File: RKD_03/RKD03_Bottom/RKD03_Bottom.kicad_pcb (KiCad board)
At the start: 2 copper layers, 97.7 x 97.6 mm, 5 parts

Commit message: RKD03 AddName
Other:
- board text added: "RKD03_v2.0"
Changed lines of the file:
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@@
 		(layer "Edge.Cuts")
 	)
+	(gr_text "RKD03_v2.0"
+		(at 59.53125 95.25 0)
+		(layer "B.SilkS")
+		(effects
+			(font
+				(size 1 1)
+				(thickness 0.1)
+			)
+			(justify left bottom mirror)
+		)
+	)
 )

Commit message: RKD03 プロット
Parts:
- added SW2: KEY_SWITCH, kbd_SW:CherryMX_stab_2u, F.Cu at (121.4, 102.4)
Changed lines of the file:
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@@
+		)
+	)
+	(footprint "kbd_SW:CherryMX_stab_2u"
+		(layer "F.Cu")
+		(at 121.44375 102.39375 180)
+		(property "Reference" "SW2"
+			(at 7 8.1 0)
+			(layer "F.SilkS")
+			(hide yes)
+			(effects
+				(font
+					(size 1 1)
+					(thickness 0.15)
+				)
+			)
+		)
+		(property "Value" "KEY_SWITCH"
+			(at -7.4 -8.1 0)
+			(layer "F.Fab")
+			(hide yes)
+			(effects
+				(font
+					(size 1 1)
+					(thickness 0.15)
+				)
+			)
+		)
+		(property "Footprint" "kbd_SW:CherryMX_stab_2u"
+			(at 0 0 0)
+			(layer "F.Fab")
+			(hide yes)
+			(effects
+				(font
+					(size 1.27 1.27)
+					(thickness 0.15)
+				)
+			)
+		)
+		(property "Datasheet" ""
+			(at 0 0 0)
+			(layer "F.Fab")
+			(hide yes)
+			(effects
+				(font
+					(size 1.27 1.27)
+					(thickness 0.15)
+				)
+			)
+		)
+		(property "Description" ""
+			(at 0 0 0)
+			(layer "F.Fab")
+			(hide yes)
+			(effects
+				(font
+					(size 1.27 1.27)
+					(thickness 0.15)
+				)
+			)
+		)
+		(attr smd)
+		(fp_line
+			(start 18 9)
+			(end -18 9)
+			(stroke
+				(width 0.15)
+				(type solid)
+			)
+			(layer "Eco2.User")
+		)
+		(fp_line
+			(start 18 -9)
+			(end 18 9)
+			(stroke
+				(width 0.15)
+				(type solid)
+			)
+			(layer "Eco2.User")
+		)
+		(fp_line
+			(start -18 9)
+			(end -18 -9)
+			(stroke
+				(width 0.15)
+				(type solid)
+			)
+			(layer "Eco2.User")
+		)
+		(fp_line
+			(start -18 -9)
+			(end 18 -9)
+			(stroke
+				(width 0.15)
+				(type solid)
+			)
+			(layer "Eco2.User")
+		)
+		(fp_line
+			(start 19.025 9.525)
+			(end 19.025 -9.525)
+			(stroke
+				(width 0.15)
+				(type solid)
+			)
+			(layer "F.Fab")
+		)
+		(fp_line
+			(start 19.025 -9.525)
+			(end -19.025 -9.525)
+			(stroke
+				(width 0.15)
+				(type solid)
+			)
+			(layer "F.Fab")
+		)
+		(fp_line
+			(start -19.025 9.525)
+			(end 19.025 9.525)
+			(stroke
+				(width 0.15)
+				(type solid)
+			)
+			(layer "F.Fab")
+		)
+		(fp_line
+			(start -19.025 -9.525)
+			(end -19.025 9.525)
+			(stroke
+				(width 0.15)
+				(type solid)
+			)
+			(layer "F.Fab")
+		)
+		(pad "" np_thru_hole circle
+			(at -11.938 -6.985)
+			(size 3.048 3.048)
+			(drill 3.048)
+			(layers "*.Cu" "*.Mask")
+		)
+		(pad "" np_thru_hole circle
+			(at -11.938 8.255)
+			(size 3.9878 3.9878)
+			(drill 3.9878)
+			(layers "*.Cu" "*.Mask")
+		)
+		(pad "" np_thru_hole circle
+			(at 11.938 -6.985)
+			(size 3.048 3.048)
+			(drill 3.048)
+			(layers "*.Cu" "*.Mask")
+		)
+		(pad "" np_thru_hole circle
+			(at 11.938 8.255)
+			(size 3.9878 3.9878)
+			(drill 3.9878)
+			(layers "*.Cu" "*.Mask")
 		)
 	)

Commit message: RKD03修正
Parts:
- added SW2: KEY_SWITCH, kbd_SW:CherryMX_stab_2u, F.Cu at (73.8, 73.8)
- added SW2: KEY_SWITCH, kbd_SW:CherryMX_stab_2u, F.Cu at (111.9, 73.8)
- added SW2: KEY_SWITCH, kbd_SW:CherryMX_stab_2u, F.Cu at (92.9, 73.8)
- added SW2: KEY_SWITCH, kbd_SW:CherryMX_stab_2u, F.Cu at (54.8, 73.8)
- moved SW2 30.1 mm to (131.0, 73.8), turned to -90 degrees

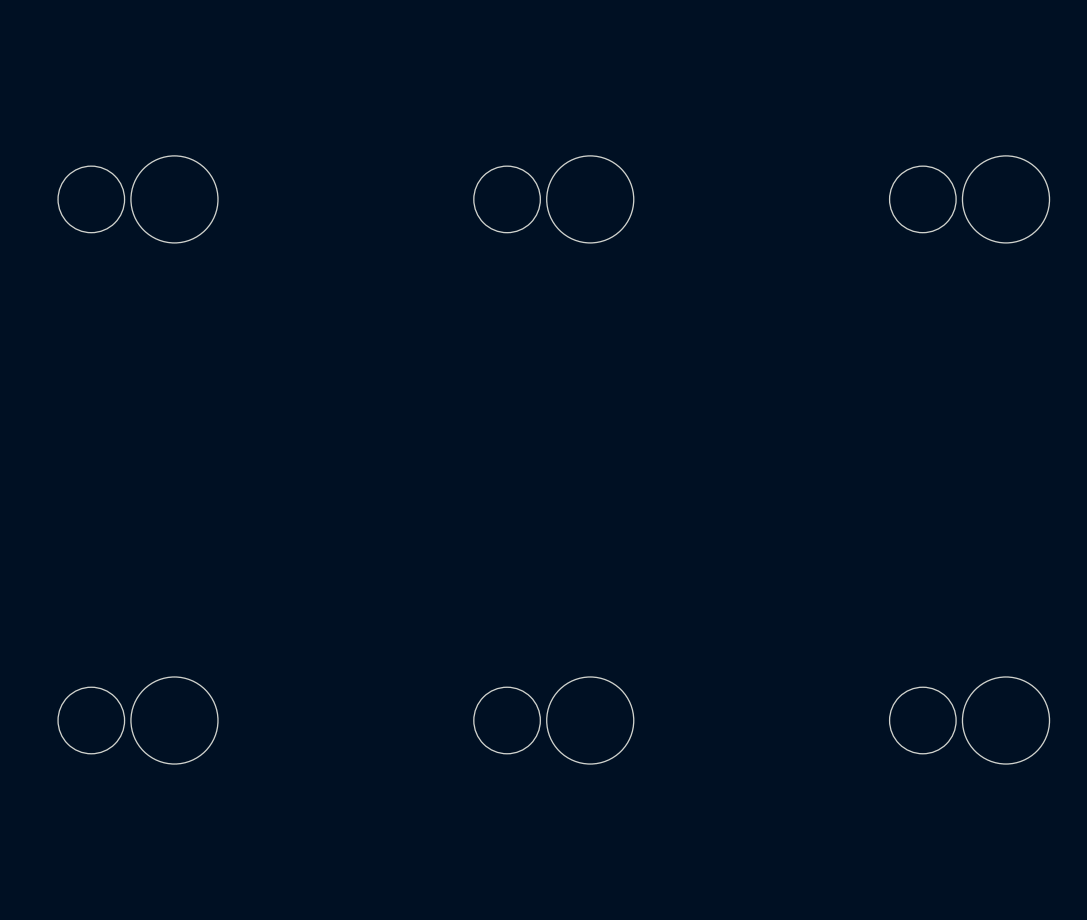
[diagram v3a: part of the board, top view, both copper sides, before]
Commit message: RKD03 2u修正
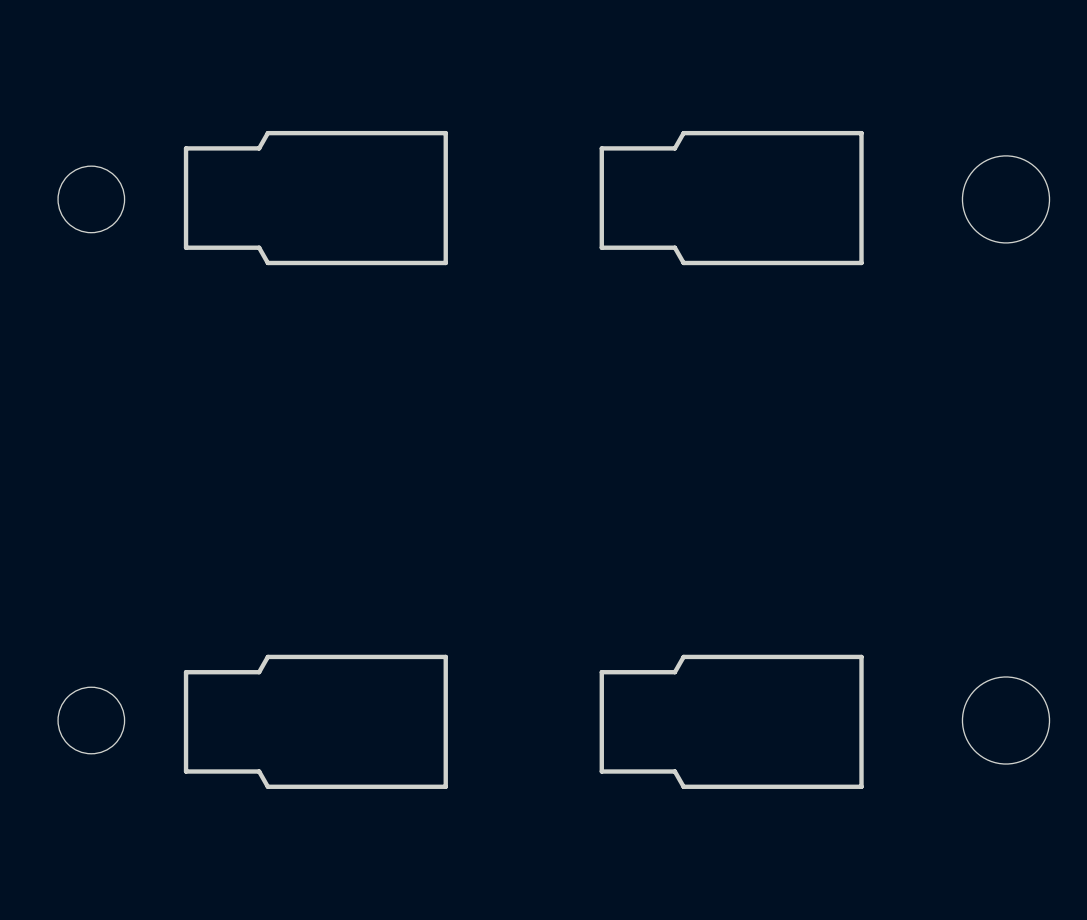
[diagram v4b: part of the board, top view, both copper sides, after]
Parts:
- SW2 (x2): footprint kbd_SW:CherryMX_stab_2u -> Rikkodo_FootPrint:rkd_Bot_ChocV2_2u
- turned SW2 to 90 degrees (x2)

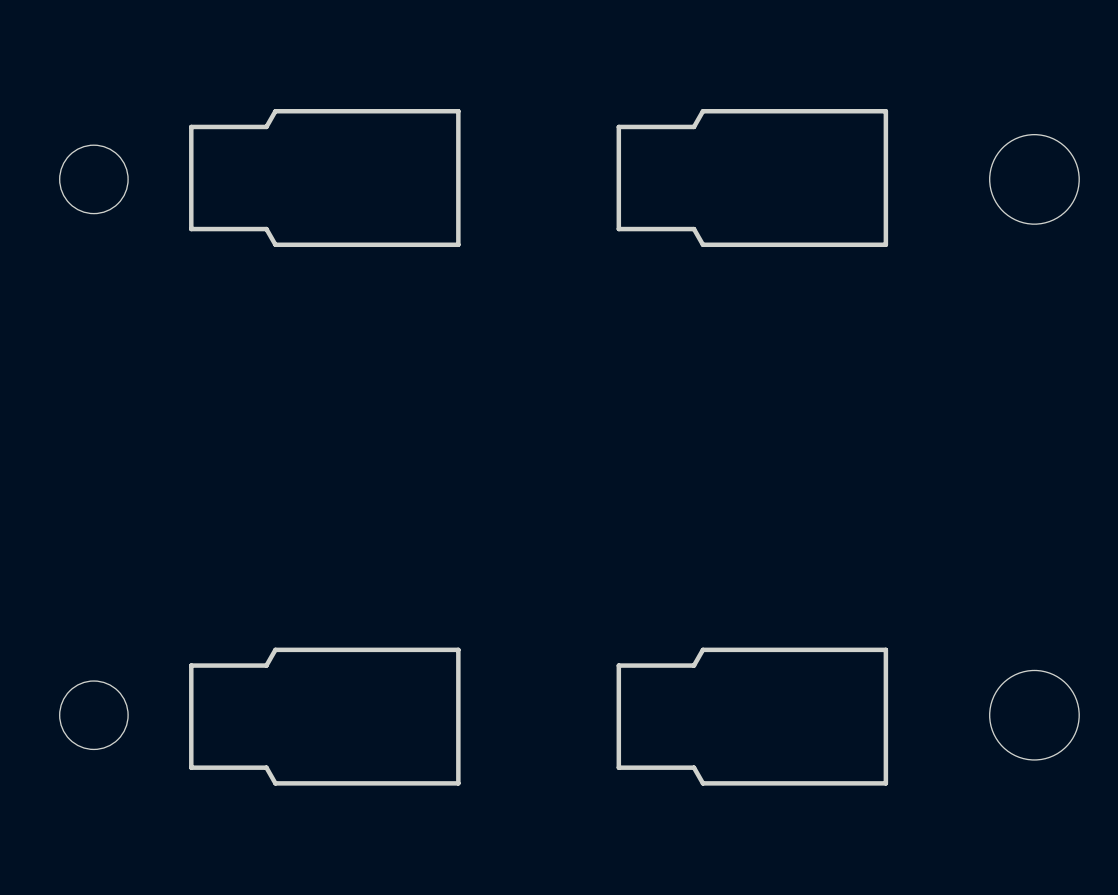
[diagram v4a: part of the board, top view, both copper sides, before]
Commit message: RKD03 部品修正
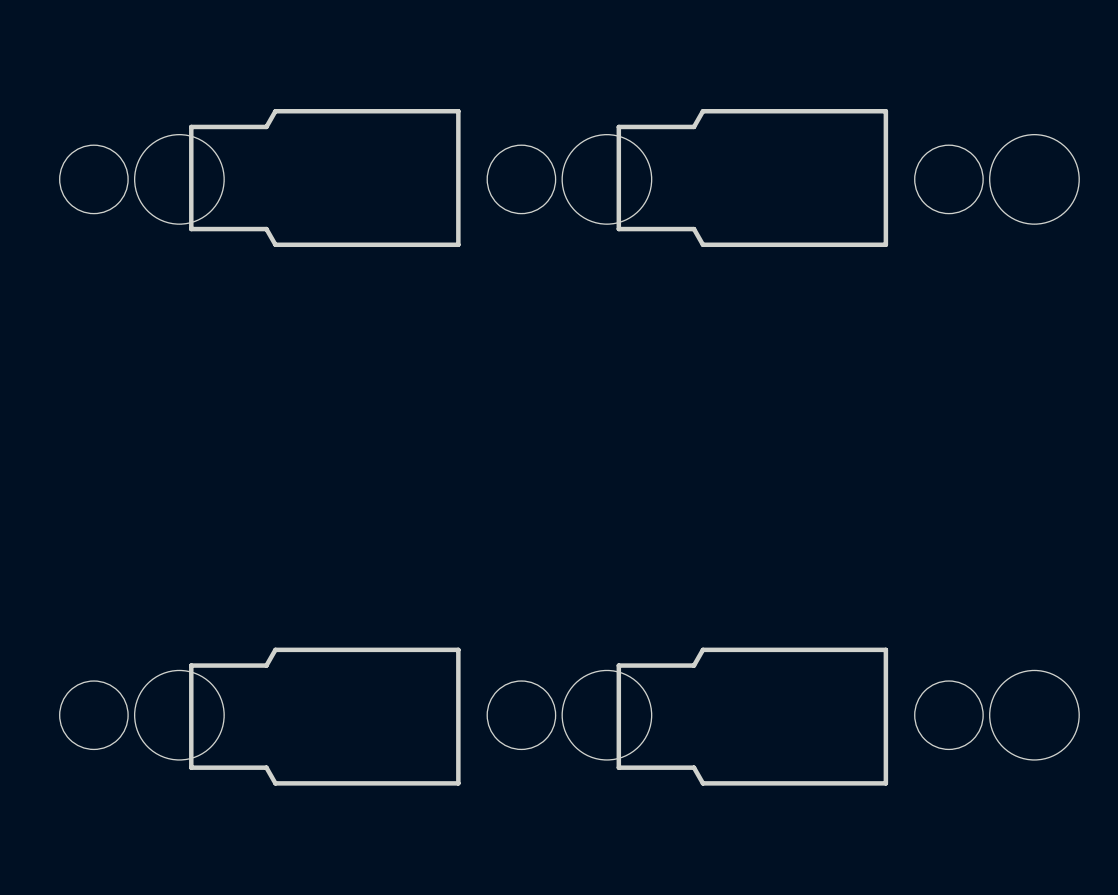
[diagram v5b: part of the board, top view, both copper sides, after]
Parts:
- added SW2: KEY_SWITCH, kbd_SW:CherryMX_stab_2u, F.Cu at (92.9, 73.8)
- added SW2: KEY_SWITCH, kbd_SW:CherryMX_stab_2u, F.Cu at (111.9, 73.8)

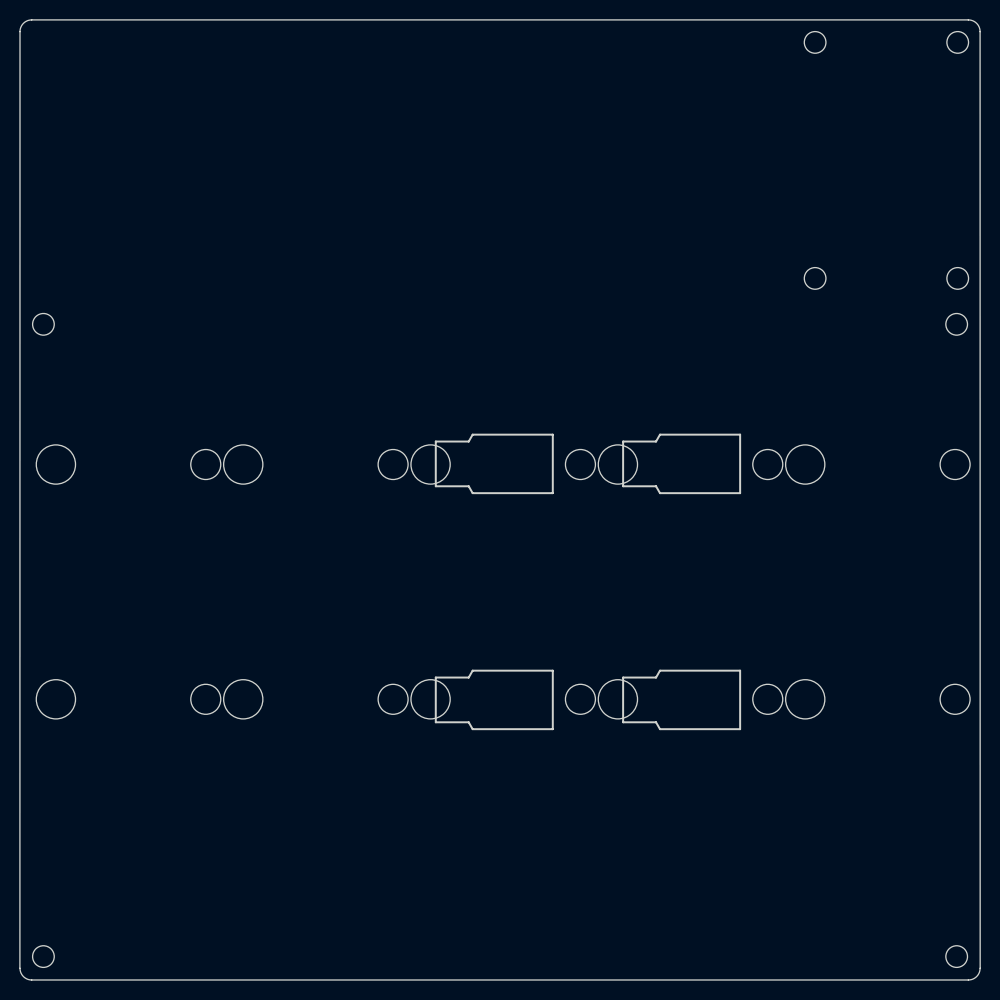
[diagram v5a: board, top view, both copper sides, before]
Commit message: RKD04対応
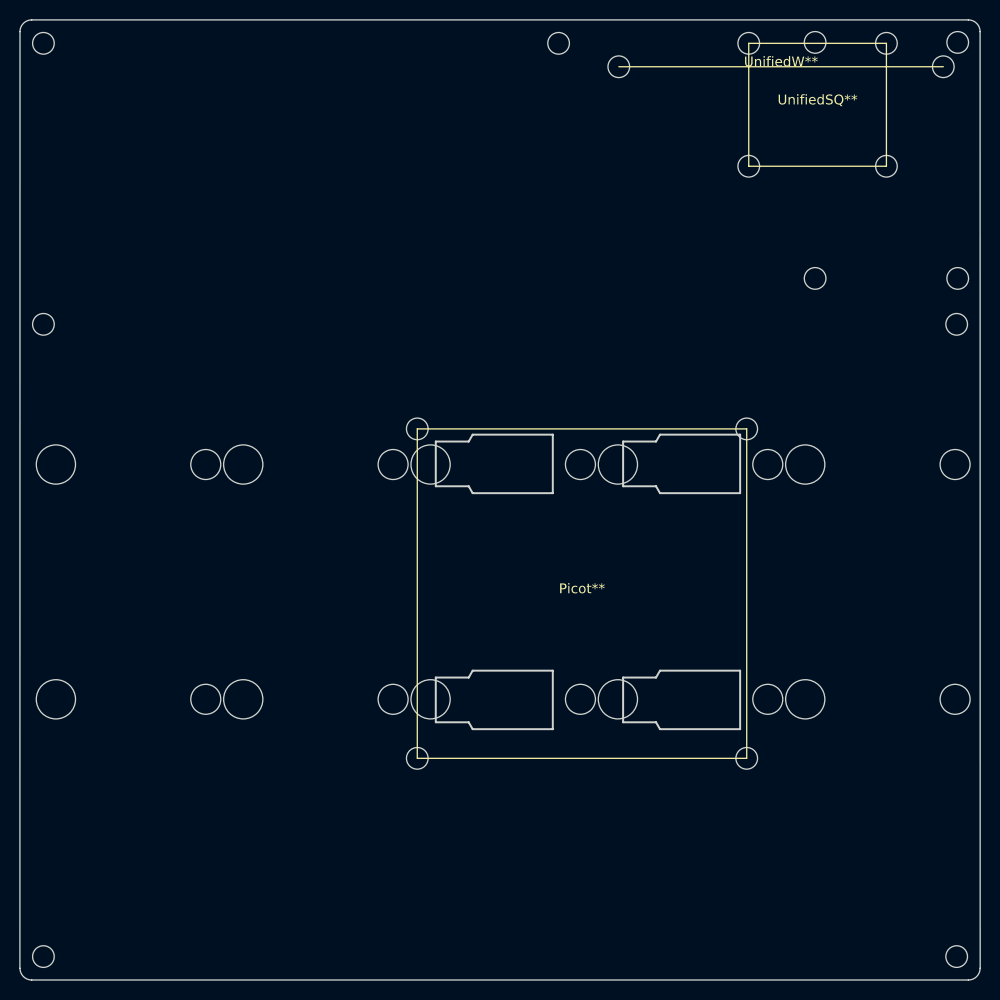
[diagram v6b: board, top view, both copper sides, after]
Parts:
- added Picot**: rkd_picot5400_BTM, Rikkodo_FootPrint:rkd_picot5400_BTM, F.Cu at (100.0, 75.0)
- added Ref**: Val**, kbd_Hole:m2_Screw_Hole, F.Cu at (97.6, 19.1)
- added Ref**: Val**, kbd_Hole:m2_Screw_Hole, F.Cu at (45.2, 19.1)
- added UnifiedSQ**: rkd_unified_sq_BTM, Rikkodo_FootPrint:rkd_unified_sq_BTM, F.Cu at (124.0, 25.3)
- added UnifiedW**: rkd_unified_wid_BTM, Rikkodo_FootPrint:rkd_unified_wid_BTM, F.Cu at (120.3, 21.4)
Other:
- board text added: "Picot"

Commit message: 04対応
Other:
- board text added: "RKD03/04_v2.0"
- board text removed: "RKD03_v2.0"
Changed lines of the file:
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@@
 		(layer "Edge.Cuts")
 	)
-	(gr_text "RKD03_v2.0"
+	(gr_text "RKD03/04_v2.0"
 		(at 59.53125 95.25 0)
 		(layer "B.SilkS")

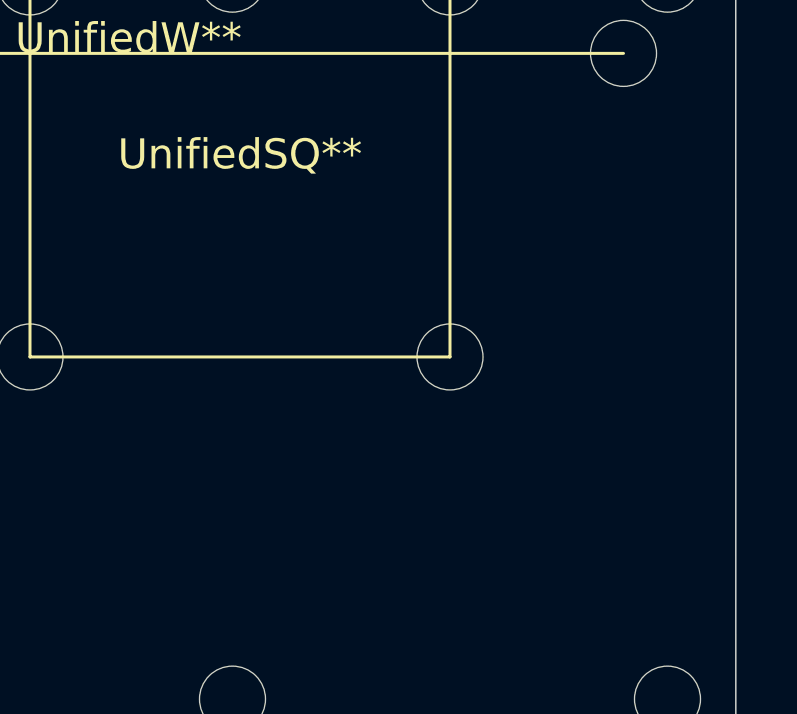
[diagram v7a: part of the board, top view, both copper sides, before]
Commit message: SekiBall追加
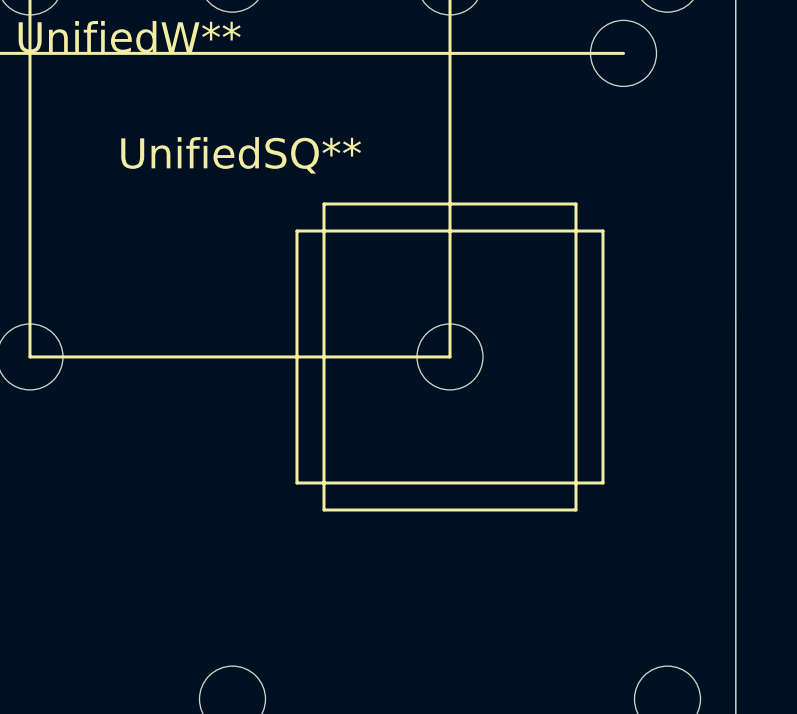
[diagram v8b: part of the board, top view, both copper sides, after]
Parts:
- added REF** (x2): rkd_SekiBall_ScrewHall, Rikkodo_FootPrint:rkd_SekiBall_ScrewHall, F.Cu at (131.0, 31.6)
